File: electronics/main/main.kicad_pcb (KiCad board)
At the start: 2 copper layers, 113 parts, among them IC1 ATMEGA8-P, J1 CABLE, J2 CABLE, J3 CABLE, J4 CABLE, J5 CABLE, J6 CABLE, J7 CABLE, J8 CABLE, P1 5v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

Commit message: fucking reset pin
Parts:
- moved P1 109.0 mm to (206.7, 67.3), turned to 270 degrees
- moved C6 106.9 mm to (217.5, 44.8), turned to 90 degrees
- moved C5 102.0 mm to (206.7, 44.5)
- moved F1 99.3 mm to (206.7, 57.1), turned to 90 degrees
- moved R29 9.42 mm to (137.8, 79.1), turned to 90 degrees
- moved C16 2.56 mm to (163.8, 85.1), turned to 180 degrees
- moved C11 2.56 mm to (154.3, 85.1), turned to 0 degrees
- moved X1 1.91 mm to (159.1, 77.8)
- moved R47 0.95 mm to (120.7, 44.8)
- moved R37 0.63 mm to (193.0, 75.2)
- moved R38 0.63 mm to (199.7, 75.2)
- moved R39 0.63 mm to (196.2, 75.2)
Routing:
- net VCC: track 397.5 -> 516.9 mm, vias 2 -> 8
- net GND: track 287.5 -> 368.3 mm
- net /RESET: track 49.3 -> 75.4 mm, vias 2 -> 4
- net Net-(F1-Pad1): track 0.00 -> 6.39 mm
- net Net-(C11-Pad1): track 10.9 -> 17.2 mm
- net Net-(C16-Pad1): track 10.6 -> 17.0 mm
- net Net-(IC1-Pad11): track 30.9 -> 34.7 mm
- net Net-(IC1-Pad12): track 28.6 -> 32.3 mm
- net /IN1: track 94.7 -> 97.3 mm
- net /IN2: track 74.9 -> 77.3 mm
- net /IN3: track 50.4 -> 52.5 mm
- net Net-(D17-Pad2): track 32.6 -> 31.7 mm
- net Net-(IC1-Pad13): track 33.7 -> 33.0 mm
- net Net-(Q7-Pad3): track 4.92 -> 5.66 mm
- net Net-(R37-Pad2): track 24.0 -> 23.4 mm
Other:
- net class Power: trace_width 1 -> 0.9

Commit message: looks finished
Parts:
- added C18: 100n, Capacitors_SMD:C_0805, B.Cu at (154.3, 73.3)
- added C19: 100n, Capacitors_ThroughHole:Capacitor6MMDiscRM5, F.Cu at (130.2, 59.7)
- moved R33 21.6 mm to (205.1, 82.9)
- moved C9 0.32 mm to (195.3, 19.7)
- moved C1 0.32 mm to (73.7, 19.7)
- moved C11 0.32 mm to (154.3, 84.8)
- moved C16 0.32 mm to (163.8, 84.8)
- moved C2 0.32 mm to (93.7, 19.7)
- moved C10 0.32 mm to (215.6, 19.7)
- moved C3 0.32 mm to (114.0, 19.7)
- moved C4 0.32 mm to (134.3, 19.7)
- moved C7 0.32 mm to (154.6, 19.7)
- moved C8 0.32 mm to (174.9, 19.7)
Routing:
- net GND: track 368.3 -> 245.9 mm
- net /BACKLIGHT: track 0.00 -> 84.7 mm, vias 0 -> 3
- net Net-(Q5-Pad2): track 10.5 -> 33.7 mm
- net VCC: track 516.9 -> 525.9 mm
- net Net-(IC1-Pad14): track 31.4 -> 30.9 mm
- added copper zone on B.Cu, net GND
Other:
- board text added: "HackFMI"

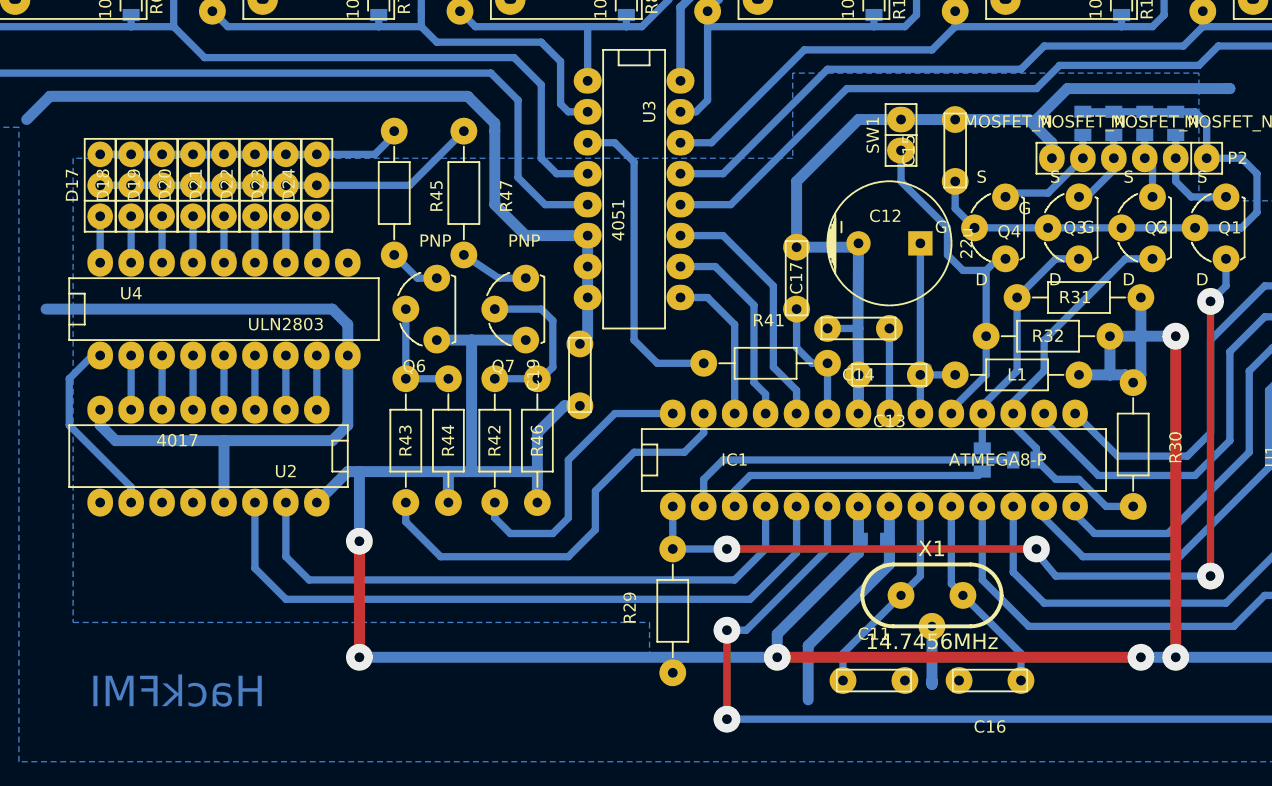
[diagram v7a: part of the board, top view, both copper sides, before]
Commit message: move jacks to components folder
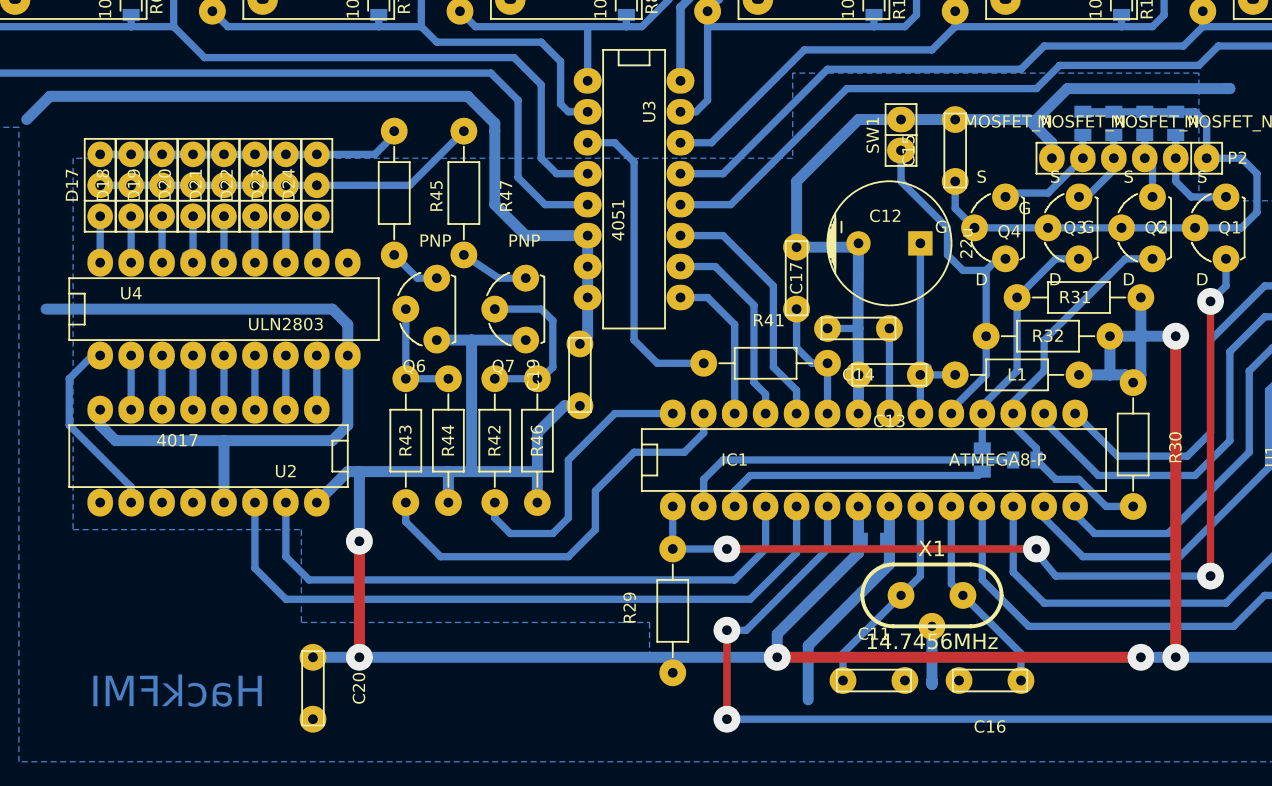
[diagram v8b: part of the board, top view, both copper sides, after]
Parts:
- added C20: 100n, Capacitors_ThroughHole:Capacitor6MMDiscRM5, F.Cu at (108.3, 85.4)
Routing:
- net VCC: track 525.9 -> 530.0 mm
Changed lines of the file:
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@@
 (kicad_pcb (version 4) (host pcbnew "(2015-11-08 BZR 6303, Git 5897580)-product")
   (general
-    (links 250)
+    (links 252)
     (no_connects 16)
     (area 0 0 0 0)
     (thickness 1.6)
     (drawings 1)
-    (tracks 544)
+    (tracks 546)
     (zones 0)
-    (modules 115)
+    (modules 116)
     (nets 85)
   )
@@
     )
   )
+  (module Capacitors_ThroughHole:Capacitor6MMDiscRM5 (layer F.Cu)
+    (at 108.2675 85.4075 270)
+    (descr "Capacitor 6MM Disc RM 5MM")
+    (tags C)
+    (fp_text reference C20 (at 0 -3.81 270) (layer F.SilkS)
+      (effects (font (size 1 1) (thickness 0.15)))
+    )
+    (fp_text value 100n (at 0 -2.286 270) (layer F.SilkS) hide
+      (effects (font (size 1 1) (thickness 0.15)))
+    )
+    (fp_line (start -3.048 -0.889) (end -3.048 0.889) (layer F.SilkS) (width 0.15))
+    (fp_line (start -3.048 0.889) (end 3.048 0.889) (layer F.SilkS) (width 0.15))
+    (fp_line (start 3.048 0.889) (end 3.048 -0.889) (layer F.SilkS) (width 0.15))
+    (fp_line (start 3.048 -0.889) (end -3.048 -0.889) (layer F.SilkS) (width 0.15))
+    (pad 1 thru_hole circle (at -2.54 0 270) (size 2.2 2.2) (drill 0.8001) (layers *.Cu *.Mask F.SilkS)
+      (net 6 VCC))
+    (pad 2 thru_hole circle (at 2.54 0 270) (size 2.2 2.2) (drill 0.8001) (layers *.Cu *.Mask F.SilkS)
+      (net 2 GND))
+    (model Capacitors_ThroughHole/Capacitor6MMDiscRM5.wrl
+      (at (xyz 0 0 0))
+      (scale (xyz 1 1 1))
+      (rotate (xyz 0 0 0))
+    )
+  )
   (gr_text HackFMI (at 97.155 85.725) (layer B.Cu)
     (effects (font (size 2.5 2.5) (thickness 0.5)) (justify mirror))
@@
   (segment (start 137.4775 28.8925) (end 135.255 31.115) (width 0.6) (layer B.Cu) (net 5))
   (segment (start 120.3325 25.715) (end 120.3325 29.845) (width 0.6) (layer B.Cu) (net 5) (status 20))
+  (segment (start 111.76 82.8675) (end 108.2675 82.8675) (width 0.9) (layer B.Cu) (net 6) (status 800000))
   (segment (start 153.035 74.295) (end 153.035 73.6125) (width 0.9) (layer B.Cu) (net 6))
   (segment (start 153.035 73.6125) (end 153.305 73.3425) (width 0.9) (layer B.Cu) (net 6))
@@
   (via (at 221.2975 48.26) (size 2.2) (drill 0.8) (layers F.Cu B.Cu) (net 6))
   (segment (start 146.3675 82.8675) (end 137.795 82.8675) (width 0.9) (layer B.Cu) (net 6))
-  (segment (start 137.795 82.8675) (end 112.0775 82.8675) (width 0.9) (layer B.Cu) (net 6))
+  (segment (start 137.795 82.8675) (end 111.76 82.8675) (width 0.9) (layer B.Cu) (net 6))
+  (segment (start 111.76 82.8675) (end 112.0775 82.8675) (width 0.9) (layer B.Cu) (net 6))
   (segment (start 112.0775 67.6275) (end 112.0775 67.945) (width 0.9) (layer B.Cu) (net 6))
   (segment (start 112.0775 73.3425) (end 112.0775 67.6275) (width 0.9) (layer B.Cu) (net 6))
@@
     )
     (polygon
-      (pts        (xy 147.6375 34.925) (xy 147.6375 41.91) (xy 88.5825 41.91) (xy 88.5825 80.01) (xy 135.89 80.01)
-        (xy 135.89 82.55) (xy 201.6125 82.55) (xy 201.6125 45.4025) (xy 180.975 45.4025) (xy 180.975 34.925)
-        (xy 154.94 34.925)
+      (pts        (xy 147.6375 34.925) (xy 147.6375 41.91) (xy 88.5825 41.91) (xy 88.5825 72.39) (xy 107.315 72.39)
+        (xy 107.315 80.01) (xy 135.89 80.01) (xy 135.89 82.55) (xy 201.6125 82.55) (xy 201.6125 45.4025)
+        (xy 180.975 45.4025) (xy 180.975 34.925) (xy 147.6375 34.925)
       )
     )
